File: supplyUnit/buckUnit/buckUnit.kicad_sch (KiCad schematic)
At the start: 23 parts

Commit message: Buck
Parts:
- C1, C3, C4, C5, C7, C8: renamed from C?; footprint 2024l2:cap0603 -> Buck:cap0603
- C2, C6: renamed from C?; footprint 2024l2:EIA-7343-D -> Buck:EIA-7343-D
- D1, D2: renamed from D?; footprint 2024l2:SMA (DO-214AC) -> Buck:SMA (DO-214AC)
- L1, L2: renamed from L?; footprint 2024l2:0630 One Piece Inductor -> Buck:0630 One Piece Inductor
- R1, R2, R3, R4: renamed from R?; footprint 2024l2:res0603 -> Buck:res0603
- U1, U2: renamed from U?; footprint 2024l2:TI_SO-PowerPAD-8 -> Buck:TI_SO-PowerPAD-8
- gave numbers to parts that had none: 5
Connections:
- net GNDREF is gone; now on net GND: J3.2 (Pin_2), J3.3 (Pin_3), J3.4 (Pin_4), J3.5 (Pin_5), J3.6 (Pin_6)

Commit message: buck
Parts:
- removed J5: Conn_01x05, symbol Connector_Generic:Conn_01x05
- added J2: Motor, Library:xt30-f, symbol Connector_Generic:Conn_01x02
- added J3: Dribbler, Connector_JST:JST_XH_B2B-XH-A_1x02_P2.50mm_Vertical, symbol Connector_Generic:Conn_01x02
- added J4: Conn_01x05, Connector_JST:JST_XH_B5B-XH-A_1x05_P2.50mm_Vertical, symbol Connector_Generic:Conn_01x05
- C1, C3, C4, C5, C7, C8: footprint Buck:cap0603 -> Library:cap0603
- C2, C6: footprint Buck:EIA-7343-D -> Library:eia-7343-d
- D1, D2: footprint Buck:SMA (DO-214AC) -> Library:SMA (DO-214AC)
- J1: value Conn_01x02 -> VBAT; footprint (none) -> Library:xt60-f
- J5: renamed from J4; value Conn_01x02 -> L1; footprint (none) -> Connector_JST:JST_XH_B2B-XH-A_1x02_P2.50mm_Vertical
- L1, L2: footprint Buck:0630 One Piece Inductor -> Library:0630 One Piece Inductor
- R1, R2, R3, R4: footprint Buck:res0603 -> Library:res0603
- U1, U2: footprint Buck:TI_SO-PowerPAD-8 -> Library:TI_SO-PowerPAD-8
- renumbered J2 to J6, J3 to J7
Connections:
- net +12V: now also J1.1 (Pin_1), J2.1 (Pin_1), J3.1 (Pin_1)
- net +3V3: now also J5.1 (Pin_1), J4.2 (Pin_2)
- net +5V: now also J4.1 (Pin_1)
- net GND: now also J1.2 (Pin_2), J5.2 (Pin_2), J2.2 (Pin_2), J3.2 (Pin_2)
- net Sol renamed KICK SIG
- net KICK SIG: now also J4.3 (Pin_3)
- new net GNDREF: J4.4 (Pin_4), J4.5 (Pin_5)
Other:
- moved on the sheet: J1, J5, J6, J7

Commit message: okl
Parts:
- removed C2, C6: 220u, Library:eia-7343-d, symbol Device:C_Polarized
- removed C3, C7: 0u1, Library:cap0603, symbol Device:C
- removed C4, C8: 10u, Library:cap0603, symbol Device:C
- removed C5: 10n, Library:cap0603, symbol Device:C
- removed D1, D2: SS54, Library:SMA (DO-214AC), symbol Diode:B340
- removed L1, L2: 15uH, Library:0630 One Piece Inductor, symbol Device:L_Iron
- removed U1, U2: TPS5430DDA, Library:TI_SO-PowerPAD-8, symbol Regulator_Switching:TPS5430DDA
- added C2: 10u, Library:cap0603, symbol Device:C
- added H1, H2, H3, H4: MountingHole, MountingHole:MountingHole_3.2mm_M3_Pad, symbol Mechanical:MountingHole
- added R5: 180, Library:res0603, symbol Device:R
- added R6: 10, Library:res0603, symbol Device:R
- added U1, U2: OKL-T6-W12-C, Library:MURATA_OKL-T-6-W12, symbol senrobo_kicad:OKL-T6-W12-C
- C1: value 10n -> 10u; LCSC C597236 -> (none)
- R1, R3: value 10K -> 1K; LCSC C25804 -> (none)
- R2: value 5K9 -> 1K; LCSC C23071 -> (none)
- R4: value 3K24 -> 330; LCSC C22994 -> (none)
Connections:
- net GNDREF is gone; now on net GND: J4.4 (Pin_4), J4.5 (Pin_5)
- net +12V: now also C1.1, C2.1, U1.2 (VIN), U2.2 (VIN)
- net +3V3: now also U1.4 (OUT), U1.5 (SENSE); no longer R1.1
- net +5V: now also U2.4 (OUT), U2.5 (SENSE); no longer R3.1
- net GND: now also C1.2, C2.2, R5.2, R6.2, U1.3 (GND), U1.7 (GND), U2.3 (GND), U2.7 (GND); no longer R2.2, R4.2
- net at R1.2: now also R3.1; no longer R2.1
- net at R3.2: now also R5.1; no longer R4.1
- new net: R1.1, U1.6 (TRIM)
- new net: R4.2, R6.1
- new net: U1.11, U1.12, U1.8
- new net: R2.2, R4.1
- new net: U2.11, U2.12, U2.8
- new net: R2.1, U2.6 (TRIM)
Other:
- moved on the sheet: J1, J2, J3, J4, J5

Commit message: buck Unit
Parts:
- added D1: BZX84C12, Package_TO_SOT_SMD:SOT-23, symbol Device:D_Zener
- added J8: Dribbler B, Connector_JST:JST_XH_B2B-XH-A_1x02_P2.50mm_Vertical, symbol Connector_Generic:Conn_01x02
- added Q1, Q2: BSC084P03NS3 G, Library:8-DFN (5x6), symbol vincent:PMOS_DGS
- added Q3: IRLML6344TRPbF, Package_TO_SOT_SMD:SOT-23, symbol Device:Q_NMOS_GSD
- added R10, R7, R8, R9: 10K, Library:res0603, symbol Device:R
- added SW1: SW_SPDT, Connector_PinHeader_2.54mm:PinHeader_1x03_P2.54mm_Vertical, symbol Switch:SW_SPDT
- J3: value Dribbler -> Dribbler A
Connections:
- net +12V: now also J8.1 (Pin_1), Q1.5 (D), Q1.6 (D), Q1.7 (D), Q1.8 (D), Q1.9 (D); no longer J2.1 (Pin_1)
- net +5V: now also SW1.1 (A)
- net GND: now also J8.2 (Pin_2), Q3.2 (S), R10.2, SW1.3 (C)
- new net: D1.1 (A), Q1.4 (G), Q2.4 (G), R8.1
- new net: D1.3 (K), Q1.1 (S), Q1.2 (S), Q1.3 (S), Q2.1 (S), Q2.2 (S), Q2.3 (S), R7.1
- new net: Q3.3 (D), R7.2, R8.2
- new net: Q3.1 (G), R10.1, R9.2
- new net: R9.1, SW1.2 (B)
- new net +12V MOTOR: J2.1 (Pin_1), Q2.5 (D), Q2.6 (D), Q2.7 (D), Q2.8 (D), Q2.9 (D)
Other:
- moved on the sheet: C1, C2, J2, R1, R2, R3, R4, R5, R6, U1, U2

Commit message: 死
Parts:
- removed R7: 10K, Library:res0603, symbol Device:R
- renumbered R8 to R7, R9 to R8, R10 to R9
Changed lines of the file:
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@@
 	)
 	(junction
-		(at 184.15 68.58)
-		(diameter 0)
-		(color 0 0 0 0)
-	)
-	(junction
 		(at 200.66 163.83)
 		(diameter 0)
@@
 	)
 	(junction
-		(at 194.31 97.79)
-		(diameter 0)
-		(color 0 0 0 0)
-	)
-	(junction
 		(at 66.04 27.94)
 		(diameter 0)
@@
 	(wire
 		(pts
-			(xy 184.15 97.79) (xy 194.31 97.79)
-		)
-		(stroke
-			(width 0)
-			(type default)
-		)
-	)
-	(wire
-		(pts
 			(xy 175.26 76.2) (xy 175.26 85.09)
 		)
@@
 	(wire
 		(pts
-			(xy 194.31 95.25) (xy 194.31 97.79)
+			(xy 194.31 95.25) (xy 194.31 100.33)
 		)
 		(stroke
@@
 	(wire
 		(pts
-			(xy 184.15 68.58) (xy 194.31 68.58)
+			(xy 180.34 68.58) (xy 194.31 68.58)
 		)
 		(stroke
@@
 	(wire
 		(pts
-			(xy 184.15 95.25) (xy 184.15 97.79)
-		)
-		(stroke
-			(width 0)
-			(type default)
-		)
-	)
-	(wire
-		(pts
 			(xy 158.75 167.64) (xy 158.75 165.1)
 		)
@@
 	(wire
 		(pts
-			(xy 180.34 68.58) (xy 184.15 68.58)
-		)
-		(stroke
-			(width 0)
-			(type default)
-		)
-	)
-	(wire
-		(pts
 			(xy 24.13 27.94) (xy 34.29 27.94)
 		)
@@
 	(wire
 		(pts
-			(xy 194.31 97.79) (xy 194.31 100.33)
-		)
-		(stroke
-			(width 0)
-			(type default)
-		)
-	)
-	(wire
-		(pts
 			(xy 163.83 152.4) (xy 163.83 157.48)
 		)
@@
 	(wire
 		(pts
-			(xy 184.15 68.58) (xy 184.15 87.63)
-		)
-		(stroke
-			(width 0)
-			(type default)
-		)
-	)
-	(wire
-		(pts
 			(xy 213.36 68.58) (xy 218.44 68.58)
 		)
@@
 	)
 	(symbol
-		(lib_id "Device:R")
-		(at 184.15 91.44 0)
-		(unit 1)
-		(exclude_from_sim no)
-		(in_bom yes)
-		(on_board yes)
-		(dnp no)
-		(fields_autoplaced yes)
-		(property "Reference" "R7"
-			(at 186.69 90.1699 0)
-			(effects
-				(font
-					(size 1.27 1.27)
-				)
-				(justify left)
-			)
-		)
-		(property "Value" "10K"
-			(at 186.69 92.7099 0)
-			(effects
-				(font
-					(size 1.27 1.27)
-				)
-				(justify left)
-			)
-		)
-		(property "Footprint" "Library:res0603"
-			(at 182.372 91.44 90)
-			(effects
-				(font
-					(size 1.27 1.27)
-				)
-				(hide yes)
-			)
-		)
-		(property "Datasheet" "~"
-			(at 184.15 91.44 0)
-			(effects
-				(font
-					(size 1.27 1.27)
-				)
-				(hide yes)
-			)
-		)
-		(property "Description" "Resistor"
-			(at 184.15 91.44 0)
-			(effects
-				(font
-					(size 1.27 1.27)
-				)
-				(hide yes)
-			)
-		)
-		(pin "1"
-		)
-		(pin "2"
-		)
-		(instances
-			(project ""
-				(path "/c34fb36c-9a91-4484-9886-3fd47b645bc8"
-					(reference "R7")
-					(unit 1)
-				)
-			)
-		)
-	)
-	(symbol
 		(lib_id "Connector_Generic:Conn_01x02")
 		(at 127 179.07 0)
@@
 		(dnp no)
 		(fields_autoplaced yes)
-		(property "Reference" "R8"
+		(property "Reference" "R7"
 			(at 196.85 90.1699 0)
 			(effects
@@
 			(project "buckUnit"
 				(path "/c34fb36c-9a91-4484-9886-3fd47b645bc8"
-					(reference "R8")
+					(reference "R7")
 					(unit 1)
 				)
@@
 		(on_board yes)
 		(dnp no)
-		(property "Reference" "R10"
+		(property "Reference" "R9"
 			(at 187.96 110.49 90)
 			(effects
@@
 			(project ""
 				(path "/c34fb36c-9a91-4484-9886-3fd47b645bc8"
-					(reference "R10")
+					(reference "R9")
 					(unit 1)
 				)
@@
 		(on_board yes)
 		(dnp no)
-		(property "Reference" "R9"
+		(property "Reference" "R8"
 			(at 175.26 102.87 90)
 			(effects
@@
 			(project ""
 				(path "/c34fb36c-9a91-4484-9886-3fd47b645bc8"
-					(reference "R9")
+					(reference "R8")
 					(unit 1)
 				)

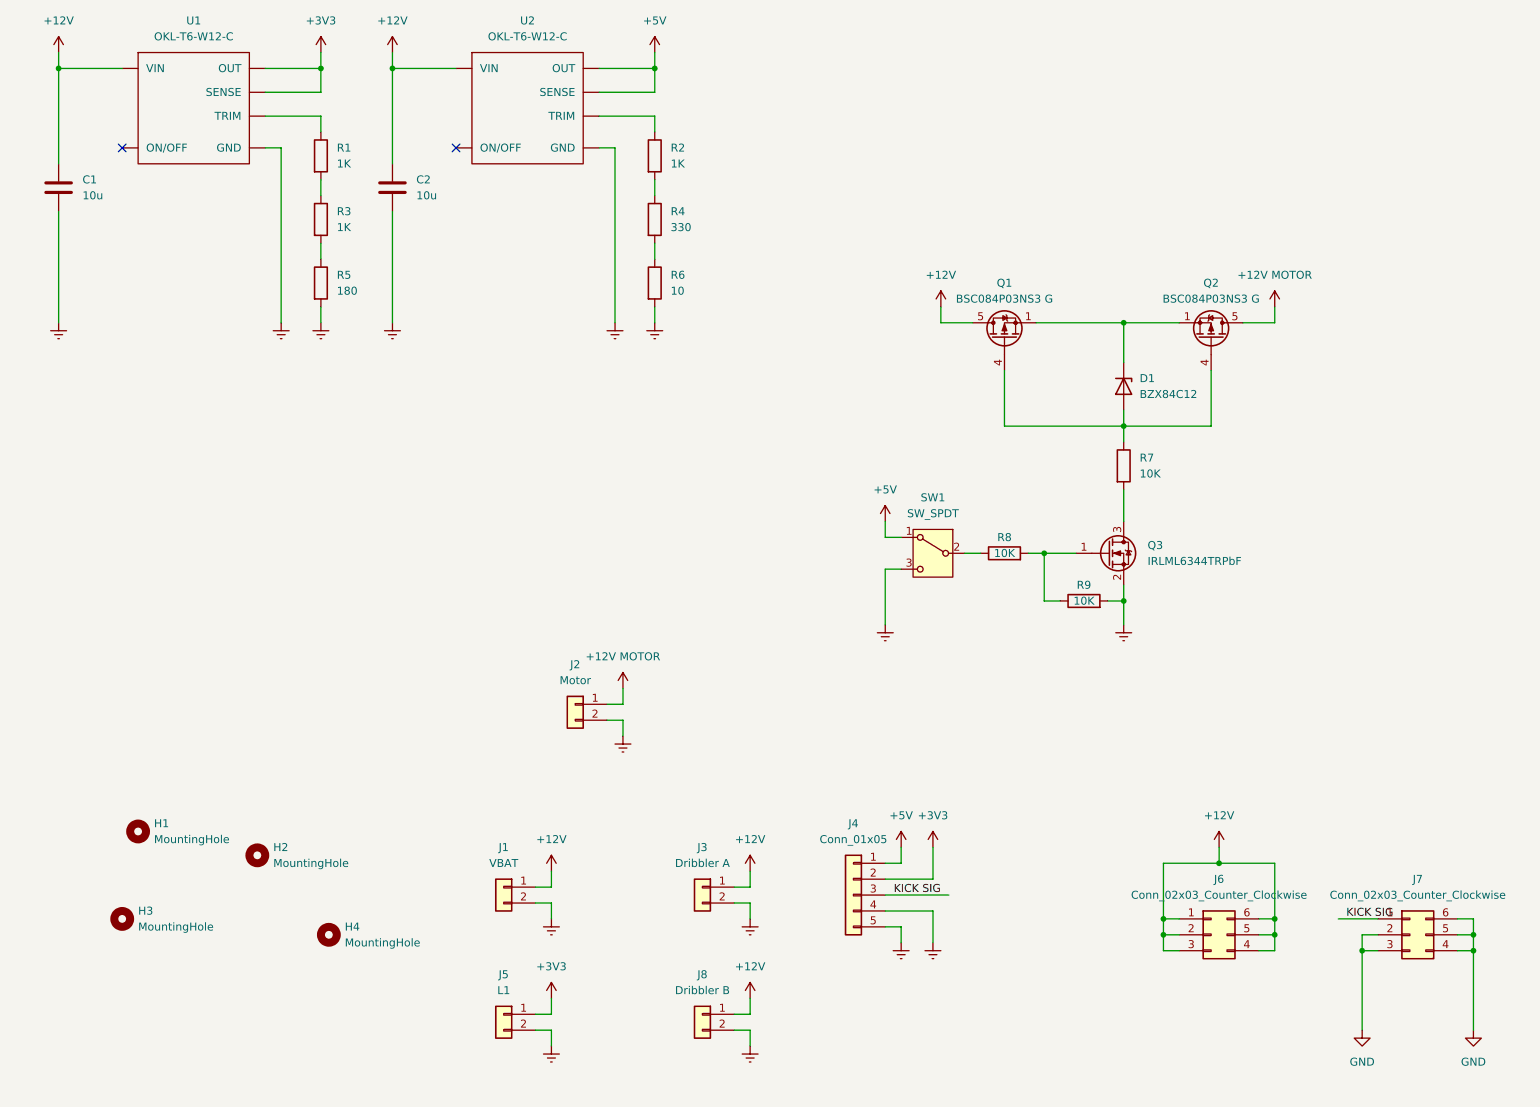
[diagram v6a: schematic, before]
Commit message: 死 - 过杀 PMOS
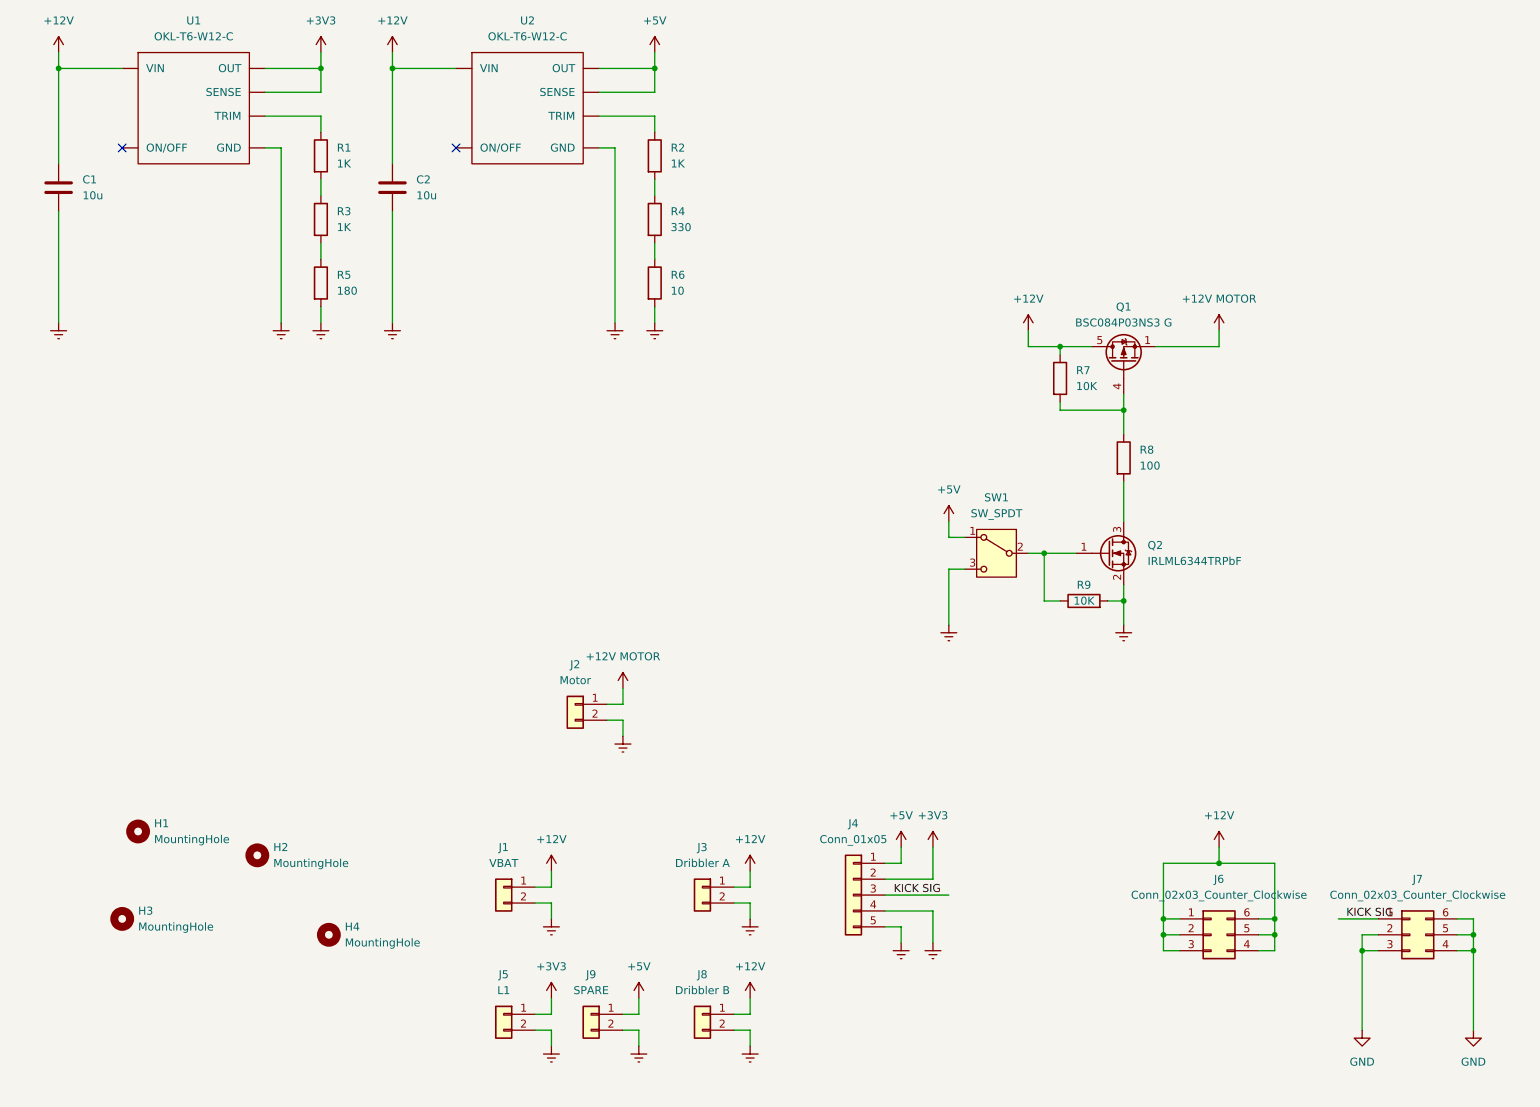
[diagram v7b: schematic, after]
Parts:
- removed D1: BZX84C12, Package_TO_SOT_SMD:SOT-23, symbol Device:D_Zener
- removed Q2: BSC084P03NS3 G, Library:8-DFN (5x6), symbol vincent:PMOS_DGS
- removed R8: 10K, Library:res0603, symbol Device:R
- added J9: SPARE, Connector_JST:JST_XH_B2B-XH-A_1x02_P2.50mm_Vertical, symbol Connector_Generic:Conn_01x02
- added R7: 10K, Library:res0603, symbol Device:R
- J3, J8: footprint Connector_JST:JST_XH_B2B-XH-A_1x02_P2.50mm_Vertical -> Library:xt30-f
- R8: renamed from R7; value 10K -> 100
- renumbered Q3 to Q2
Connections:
- net +12V: now also R7.1
- net +12V MOTOR: now also Q1.1 (S), Q1.2 (S), Q1.3 (S)
- net +5V: now also J9.1 (Pin_1)
- net GND: now also J9.2 (Pin_2)
- net at Q1.4 (G), R8.1: now also R7.2
- net at Q2.1 (G), R9.1: now also SW1.2 (B)
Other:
- moved on the sheet: Q1, R8, SW1

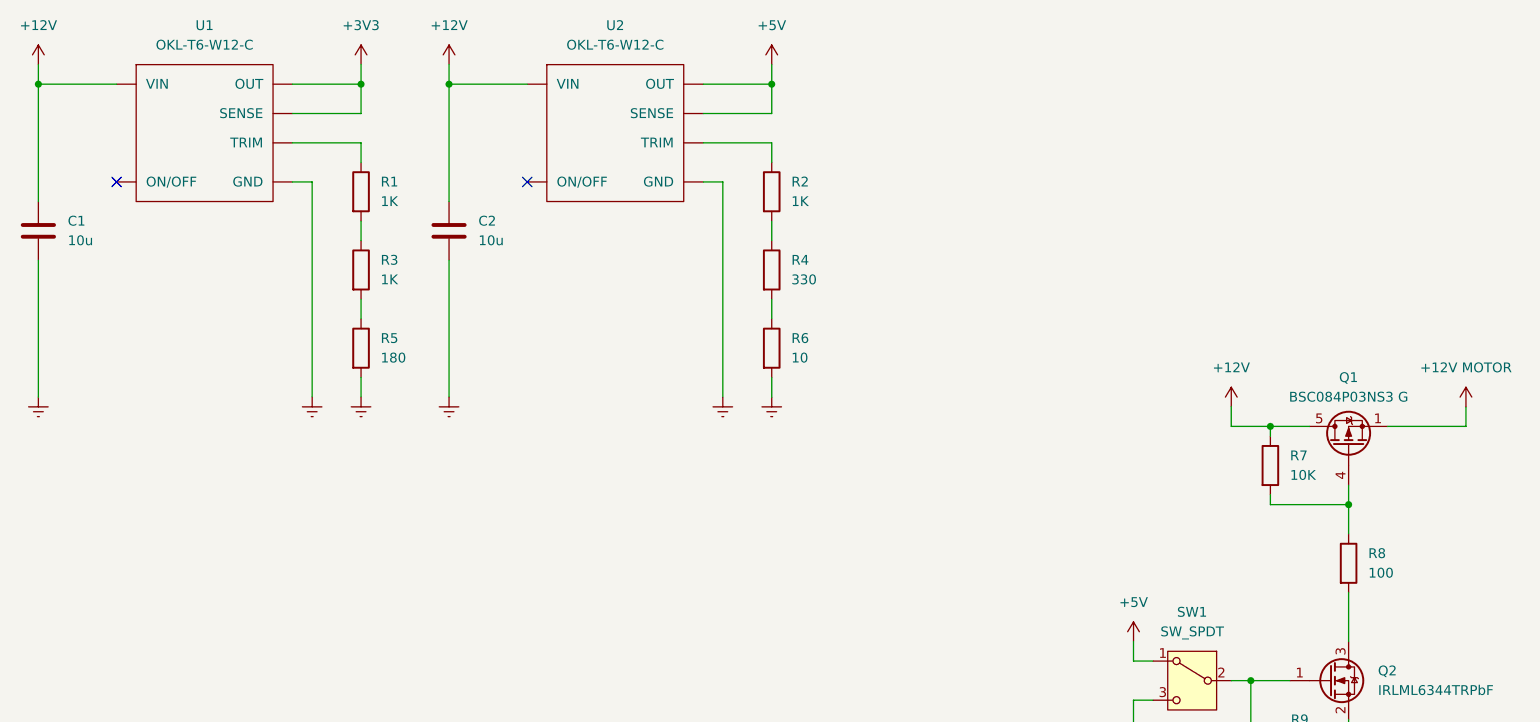
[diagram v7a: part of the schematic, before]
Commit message: 死 - 过杀 PMOS
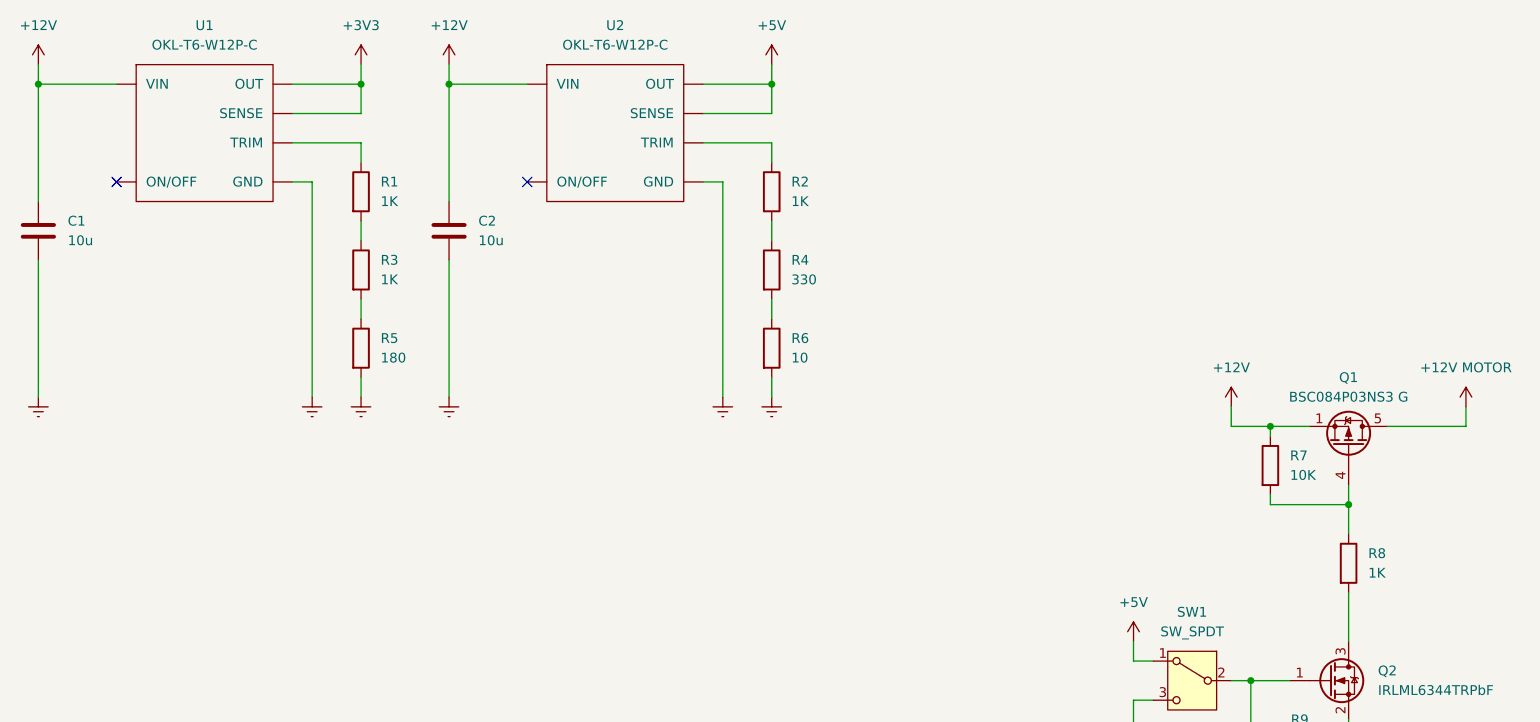
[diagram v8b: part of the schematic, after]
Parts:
- R8: value 100 -> 1K
- U1, U2: value OKL-T6-W12-C -> OKL-T6-W12P-C
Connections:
- net +12V: now also Q1.1 (S), Q1.2 (S), Q1.3 (S); no longer Q1.5 (D), Q1.6 (D), Q1.7 (D), Q1.8 (D), Q1.9 (D)
- net +12V MOTOR: now also Q1.5 (D), Q1.6 (D), Q1.7 (D), Q1.8 (D), Q1.9 (D); no longer Q1.1 (S), Q1.2 (S), Q1.3 (S)
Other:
- moved on the sheet: Q1
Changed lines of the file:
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@@
 	(symbol
 		(lib_id "vincent:PMOS_DGS")
-		(at 194.31 74.93 90)
-		(unit 1)
-		(exclude_from_sim no)
-		(in_bom yes)
-		(on_board yes)
-		(dnp no)
-		(fields_autoplaced yes)
+		(at 194.31 74.93 270)
+		(mirror x)
+		(unit 1)
+		(exclude_from_sim no)
+		(in_bom yes)
+		(on_board yes)
+		(dnp no)
 		(property "Reference" "Q1"
 			(at 194.31 66.04 90)
@@
 		)
 		(property "Footprint" "Library:8-DFN (5x6)"
-			(at 191.77 69.85 0)
+			(at 196.85 69.85 0)
 			(effects
 				(font
@@
 			)
 		)
-		(property "Value" "OKL-T6-W12-C"
+		(property "Value" "OKL-T6-W12P-C"
 			(at 45.72 22.86 0)
 			(effects
@@
 			)
 		)
-		(property "Value" "100"
+		(property "Value" "1K"
 			(at 196.85 91.4399 0)
 			(effects
@@
 			)
 		)
-		(property "Value" "OKL-T6-W12-C"
+		(property "Value" "OKL-T6-W12P-C"
 			(at 99.06 22.86 0)
 			(effects
